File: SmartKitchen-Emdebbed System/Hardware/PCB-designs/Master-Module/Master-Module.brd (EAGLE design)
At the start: 160 x 100 mm, 12 parts, among them IC2 7805DT, J1 RJ11-2L-B, J2 RJ11-2L-B, J3 RJ11-2L-B, X1 K375M

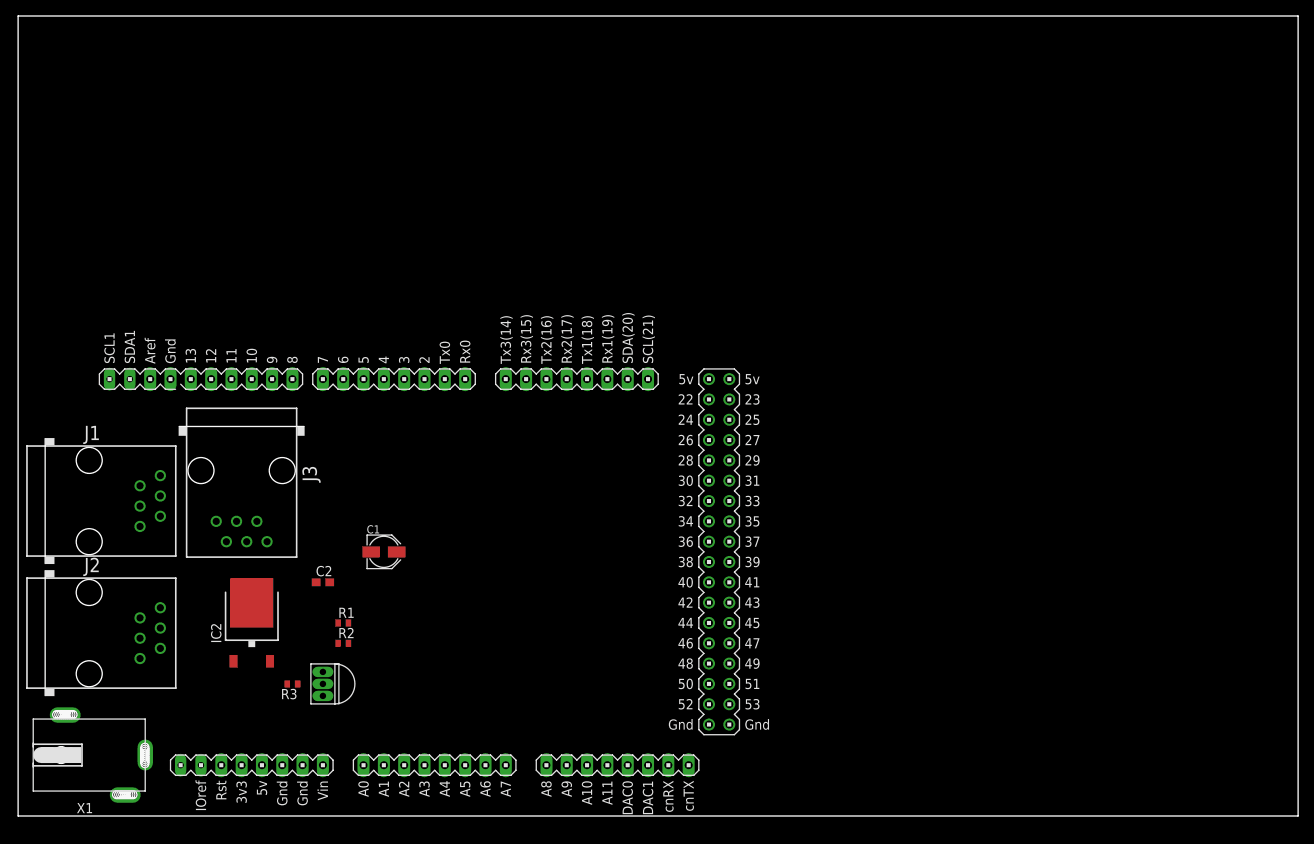
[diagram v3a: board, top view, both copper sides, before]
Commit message: Finnishing DUE shield
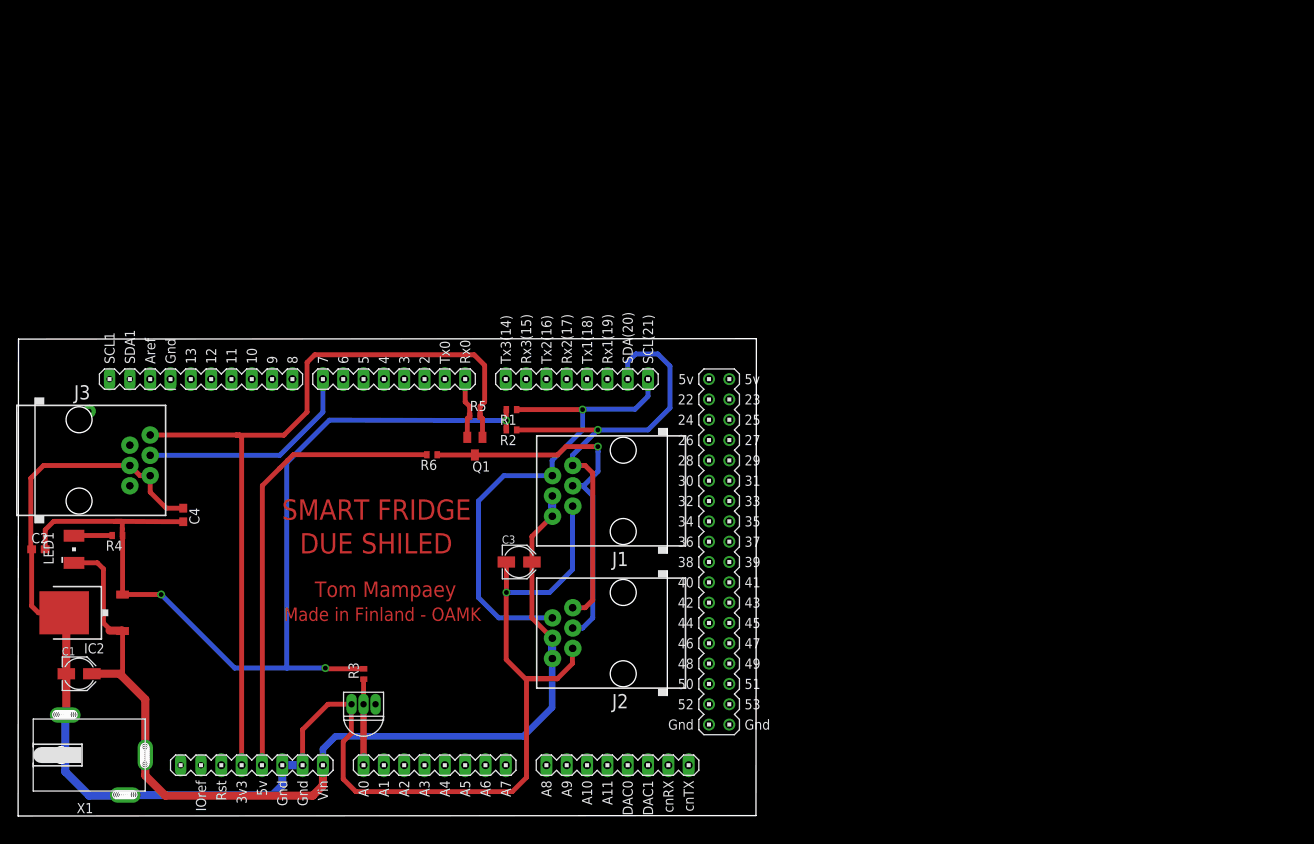
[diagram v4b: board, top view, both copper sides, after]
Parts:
- added C3: 4µ7, resistor:PANASONIC_B
- added C4: 100n, resistor:C0603
- added LED1: LG_T679-E1F1-1, led:PLCC2
- added Q1: BSS123, transistor-small-signal:SOT23
- added R4: 4k7, rcl:R0402
- added R5, R6: 10k, rcl:R0402
- moved J1 66.8 mm to (75.6, 40.6), turned to 90 degrees
- moved J2 66.8 mm to (75.6, 22.9), turned to 90 degrees
- moved C1 41.0 mm to (7.62, 17.8)
- moved C2 35.8 mm to (2.54, 33.3)
- moved R1 34.0 mm to (61.7, 50.8), turned to 180 degrees
- moved R2 34.0 mm to (61.7, 48.3), turned to 180 degrees
- moved IC2 21.0 mm to (8.26, 25.4), turned to 90 degrees
- moved J3 20.4 mm to (7.62, 44.5), turned to 270 degrees
- moved R3 9.00 mm to (43.2, 17.8), turned to 90 degrees
- moved U$2 5.68 mm to (43.2, 14.0), turned to 270 degrees
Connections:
- new net N$14: J3.1, Q1.1, R5.2, U$1.3V3
- new net N$7: LED1.A, R4.2
- new net N$8: C2.2, C4.2, IC2.2, R1.2, R2.2, R3.2, R4.1
- new net N$9: Q1.2, R5.1, U$1.RX0
- net AGND: now also C3.-, C4.1
- net N$10: now also C3.+, LED1.C
- net N$2: now also Q1.3, R6.1; no longer U$1.RX0
- net N$4: now also R6.2, U$1.5V; no longer C2.2, IC2.2, J3.1, R1.2, R2.2, R3.2
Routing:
- net AGND: track 0.00 -> 202.8 mm, vias 0 -> 1
- net N$8: track 0.00 -> 124.8 mm, vias 0 -> 3
- net N$10: track 0.00 -> 124.5 mm
- net N$14: track 0.00 -> 101.3 mm, vias 0 -> 1
- net N$3: track 0.00 -> 61.9 mm, vias 0 -> 1
- net N$1: track 0.00 -> 61.5 mm, vias 0 -> 1
- net N$4: track 0.00 -> 57.1 mm
- net N$2: track 0.00 -> 47.7 mm, vias 0 -> 1
- net N$6: track 0.00 -> 28.0 mm
- net N$5: track 0.00 -> 10.8 mm
- net N$9: track 0.00 -> 7.64 mm
- net N$7: track 0.00 -> 4.78 mm
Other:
- board size 160 x 100 mm -> 92.3 x 59.7 mm
- board text added: "DUE SHILED"
- board text added: "Made in Finland - OAMK"
- board text added: "SMART FRIDGE"
- board text added: "Tom Mampaey"

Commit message: Fine tunning
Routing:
- net N$8: track 124.8 -> 111.6 mm
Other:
- board text added: "12V DC"
- board text added: "I2C BUS"
- board text added: "SENSOR"
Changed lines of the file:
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@@
 <setting verticaltext="up"/>
 </settings>
-<grid distance="0.005" unitdist="inch" unit="inch" style="lines" multiple="1" display="no" altdistance="0.025" altunitdist="inch" altunit="inch"/>
+<grid distance="0.001" unitdist="inch" unit="inch" style="lines" multiple="1" display="no" altdistance="0.025" altunitdist="inch" altunit="inch"/>
 <layers>
 <layer number="1" name="Top" color="4" fill="1" visible="yes" active="yes"/>
@@
 <text x="37.084" y="27.3812" size="1.9304" layer="1">Tom Mampaey</text>
 <text x="33.2232" y="24.384" size="1.6764" layer="1">Made in Finland - OAMK</text>
+<text x="1.651" y="21.971" size="1.778" layer="1" rot="SR270">12V DC</text>
+<text x="68.7578" y="10.6934" size="1.778" layer="1" rot="SR0">I2C BUS</text>
+<text x="9.2456" y="55.2958" size="1.27" layer="1" rot="SR180">SENSOR</text>
 </plain>
 <attributes>
@@
 <wire x1="38.481" y1="18.415" x2="38.4048" y2="18.4912" width="0.6096" layer="1"/>
 <via x="38.4048" y="18.4912" extent="1-16" drill="0.6" shape="square"/>
-<wire x1="38.4048" y1="18.4912" x2="33.6296" y2="18.4912" width="0.6096" layer="16"/>
-<wire x1="33.6296" y1="18.4912" x2="27.0764" y2="18.4912" width="0.6096" layer="16"/>
-<wire x1="27.0764" y1="18.4912" x2="17.8816" y2="27.686" width="0.6096" layer="16"/>
 <via x="17.8816" y="27.686" extent="1-16" drill="0.6" shape="square"/>
 <wire x1="17.8816" y1="27.686" x2="13.061" y2="27.686" width="0.6096" layer="1"/>
@@
 <wire x1="61.0108" y1="49.5808" x2="61.0108" y2="49.4284" width="0.6096" layer="1"/>
 <via x="61.0108" y="49.4284" extent="1-16" drill="0.6" shape="square"/>
-<wire x1="61.0108" y1="49.4284" x2="38.9128" y2="49.4792" width="0.6096" layer="16"/>
-<wire x1="38.9128" y1="49.4792" x2="33.5788" y2="44.1452" width="0.6096" layer="16"/>
-<wire x1="33.5788" y1="44.1452" x2="33.5788" y2="18.542" width="0.6096" layer="16"/>
-<wire x1="33.5788" y1="18.542" x2="33.6296" y2="18.4912" width="0.6096" layer="16"/>
+<wire x1="61.0108" y1="49.4284" x2="51.7144" y2="49.4284" width="0.6096" layer="16"/>
+<wire x1="51.7144" y1="49.4284" x2="38.354" y2="36.068" width="0.6096" layer="16"/>
+<wire x1="38.354" y1="36.068" x2="38.354" y2="27.3812" width="0.6096" layer="16"/>
+<wire x1="38.354" y1="27.3812" x2="38.354" y2="18.542" width="0.6096" layer="16"/>
+<wire x1="38.354" y1="18.542" x2="38.4048" y2="18.4912" width="0.6096" layer="16"/>
+<wire x1="17.8816" y1="27.686" x2="38.0492" y2="27.686" width="0.6096" layer="16"/>
+<wire x1="38.0492" y1="27.686" x2="38.354" y2="27.3812" width="0.6096" layer="16"/>
 </signal>
 <signal name="N$9">
@@
 <wire x1="34.3916" y1="45.1612" x2="33.6654" y2="44.435" width="0.6096" layer="1"/>
 </signal>
-<signal name="N$11">
-<via x="8.89" y="50.5968" extent="1-16" drill="0.6" diameter="1.6764" shape="octagon"/>
-</signal>
 <signal name="N$12">
 <via x="13.97" y="46.355" extent="1-16" drill="0.9" diameter="2.1844" shape="octagon"/>
@@
 </signal>
 <signal name="N$26">
-<via x="69.342" y="20.955" extent="1-16" drill="0.9" diameter="2.1844" shape="octagon"/>
 <via x="66.802" y="19.685" extent="1-16" drill="0.9" diameter="2.1844" shape="octagon"/>
 </signal>
@@
 <via x="66.802" y="24.765" extent="1-16" drill="0.9" diameter="2.1844" shape="octagon"/>
 </signal>
+<signal name="N$29">
+<via x="69.2912" y="20.955" extent="1-16" drill="1" diameter="2.1844" shape="octagon"/>
+</signal>
 </signals>

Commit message: Adding planes and references
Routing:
- net AGND: track 202.8 -> 204.5 mm, vias 1 -> 7
- added copper zone on layer 1, net AGND
- added copper zone on layer 16, net AGND
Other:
- board text added: "DUE SHIELD"
- board text removed: "DUE SHILED"
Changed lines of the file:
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@@
 <wire x1="0.0508" y1="59.614" x2="0" y2="0" width="0" layer="20"/>
 <text x="32.9692" y="37.0332" size="2.54" layer="1">SMART FRIDGE</text>
-<text x="35.2044" y="32.8168" size="2.54" layer="1">DUE SHILED</text>
 <text x="37.084" y="27.3812" size="1.9304" layer="1">Tom Mampaey</text>
 <text x="33.2232" y="24.384" size="1.6764" layer="1">Made in Finland - OAMK</text>
@@
 <text x="68.7578" y="10.6934" size="1.778" layer="1" rot="SR0">I2C BUS</text>
 <text x="9.2456" y="55.2958" size="1.27" layer="1" rot="SR180">SENSOR</text>
+<text x="35.5092" y="33.0708" size="2.54" layer="1">DUE SHIELD</text>
 </plain>
 <attributes>
@@
 <wire x1="33.02" y1="3.81" x2="33.02" y2="6.35" width="1.016" layer="16"/>
 <wire x1="35.56" y1="6.35" x2="33.02" y2="6.35" width="1.016" layer="16"/>
-<wire x1="5.89" y1="12.62" x2="5.89" y2="5.54" width="1.016" layer="16"/>
-<wire x1="5.89" y1="5.54" x2="8.89" y2="2.54" width="1.016" layer="16"/>
-<wire x1="8.89" y1="2.54" x2="13.31" y2="2.54" width="1.016" layer="16"/>
 <wire x1="13.31" y1="2.54" x2="13.39" y2="2.62" width="1.016" layer="16"/>
 <wire x1="6.02" y1="17.78" x2="6.02" y2="12.75" width="1.016" layer="1"/>
@@
 <wire x1="61.0108" y1="19.558" x2="61.0108" y2="27.9146" width="0.6096" layer="1"/>
 <wire x1="61.0108" y1="27.9146" x2="61.0362" y2="27.94" width="0.6096" layer="1"/>
+<wire x1="5.89" y1="12.62" x2="9.4742" y2="12.62" width="1.27" layer="16"/>
+<wire x1="9.4742" y1="12.62" x2="9.4742" y2="2.667" width="1.27" layer="16"/>
+<wire x1="9.4742" y1="2.667" x2="13.39" y2="2.667" width="1.27" layer="16"/>
+<wire x1="13.39" y1="2.667" x2="13.39" y2="2.62" width="1.27" layer="16"/>
+<polygon width="0.6096" layer="16">
+<vertex x="0.0508" y="59.6138"/>
+<vertex x="92.2274" y="59.6138"/>
+<vertex x="92.2274" y="0.0508"/>
+<vertex x="0.0508" y="0.0508"/>
+</polygon>
+<polygon width="0.6096" layer="1" isolate="0.6096">
+<vertex x="0.0508" y="59.6138"/>
+<vertex x="92.2274" y="59.6138"/>
+<vertex x="92.2274" y="0.0508"/>
+<vertex x="0.0254" y="0.0508"/>
+<vertex x="0.0254" y="59.6138"/>
+</polygon>
+<via x="20.447" y="20.6502" extent="1-16" drill="0.6" shape="square"/>
+<via x="5.3848" y="57.277" extent="1-16" drill="0.6" shape="square"/>
+<via x="44.196" y="49.403" extent="1-16" drill="0.6" shape="square"/>
+<via x="68.58" y="31.7246" extent="1-16" drill="0.6" shape="square"/>
+<via x="36.3982" y="42.799" extent="1-16" drill="0.6" shape="square"/>
+<via x="65.7606" y="46.6598" extent="1-16" drill="0.6" shape="square"/>
 </signal>
 <signal name="N$5">

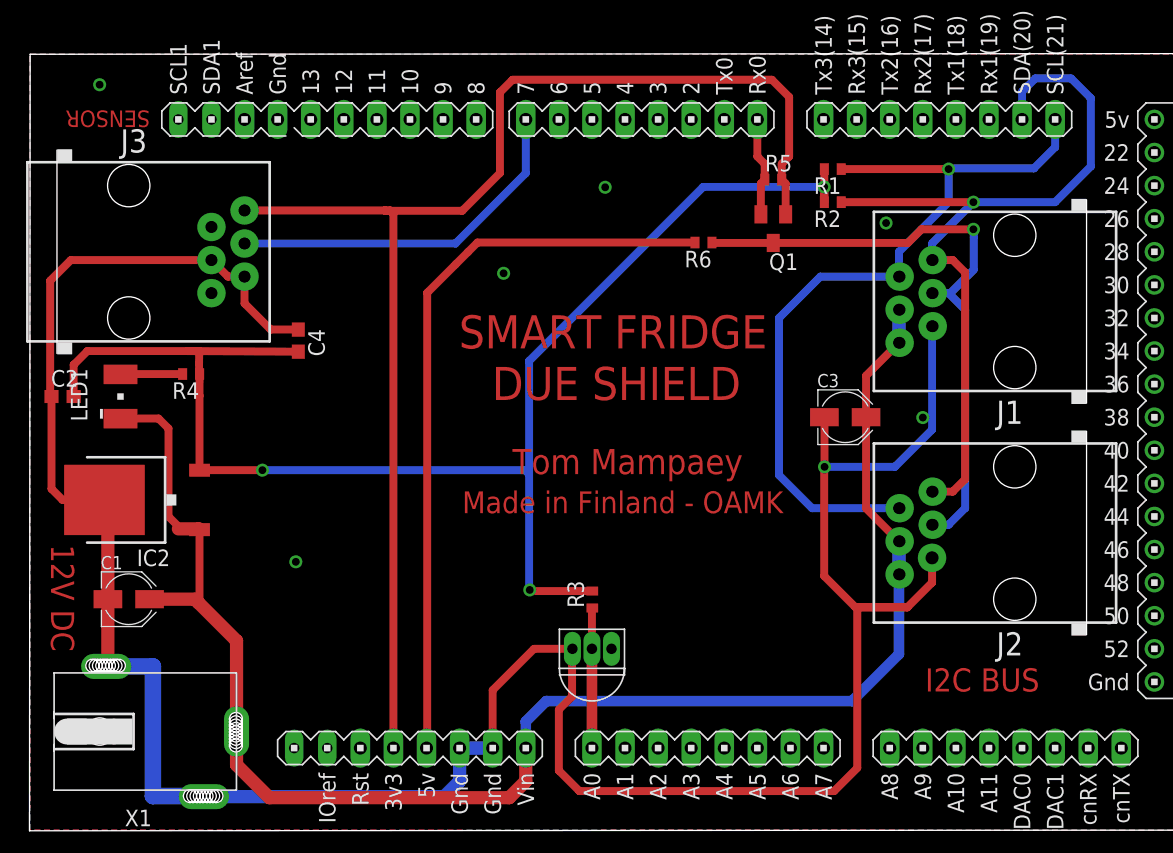
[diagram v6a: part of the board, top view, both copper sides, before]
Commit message: Complete redesing Master for Wifi-port
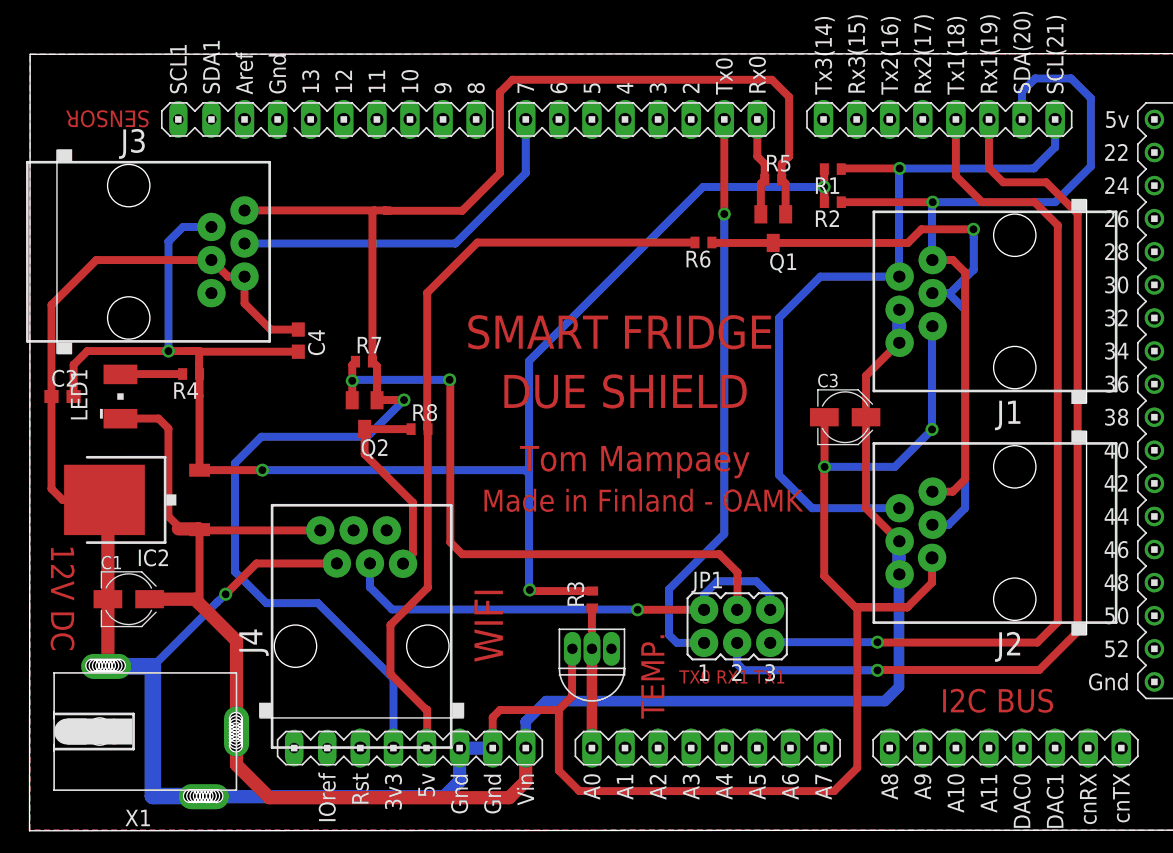
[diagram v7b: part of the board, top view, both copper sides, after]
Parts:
- added J4: RJ11-2L-B, con-tycoelectronics:RJ11-NO_SHIELD
- added JP1: (no value), jumper:JP3Q
- added Q2: BSS123, transistor-small-signal:SOT23
- added R7, R8: 10k, rcl:R0402
- R4: value 4k7 -> 1k
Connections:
- new net N$11: JP1.1, U$1.TX0
- new net N$30: JP1.3, U$1.RX1
- new net N$31: JP1.5, U$1.TX1
- new net N$33: J4.4, JP1.2, JP1.6
- new net N$34: J4.6, Q2.3, R8.1
- new net N$35: JP1.4, Q2.2, R7.1
- net AGND: now also J4.2
- net N$10: now also J4.1
- net N$14: now also Q2.1, R7.2
- net N$4: now also R8.2
- net N$8: now also J3.2
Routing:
- net N$30: track 0.00 -> 73.3 mm, vias 0 -> 1
- net N$31: track 0.00 -> 66.9 mm, vias 0 -> 1
- net N$35: track 0.00 -> 49.0 mm, vias 0 -> 2
- net N$11: track 0.00 -> 44.3 mm, vias 0 -> 1
- net N$33: track 0.00 -> 36.4 mm, vias 0 -> 1
- net N$14: track 101.3 -> 121.0 mm, vias 1 -> 2
- net N$34: track 0.00 -> 15.8 mm
- net AGND: track 204.5 -> 216.5 mm, vias 7 -> 3
- net N$8: track 111.6 -> 122.8 mm, vias 3 -> 4
- net N$10: track 124.5 -> 135.3 mm
- net N$4: track 57.1 -> 59.6 mm
- net N$3: track 61.9 -> 60.4 mm
- net N$1: track 61.5 -> 60.2 mm
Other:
- board text added: "TEMP."
- board text added: "TX0 RX1 TX1"
- board text added: "WIFI"
